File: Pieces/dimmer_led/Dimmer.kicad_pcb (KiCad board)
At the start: 2 copper layers, 67 x 56 mm, 41 parts, among them J1 Conn_01x02_Female, J2 Conn_01X03, J3 TB_1X2, J4 Conn_01x03_Female, J5 TB_1X2, J6 TB_1X2, Q1 BTA06-600C, Q2 BTA06-600C, Q3 BTA06-600C, Q5 2N7000, U1 LM78XX, U14 LM324, U3 MOC3020M, U4 MOC3020M, U5 MOC3020M, U7 PC817

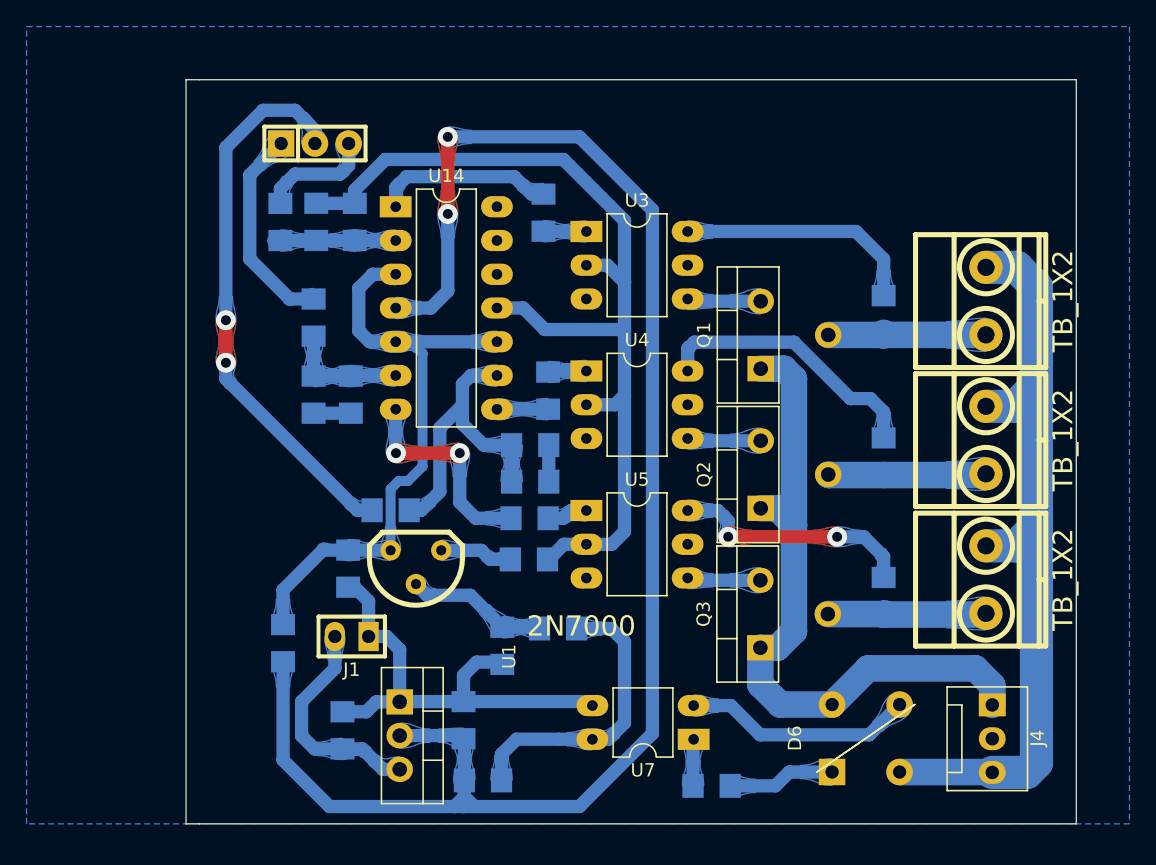
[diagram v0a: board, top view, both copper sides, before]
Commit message: dimmer actualizado
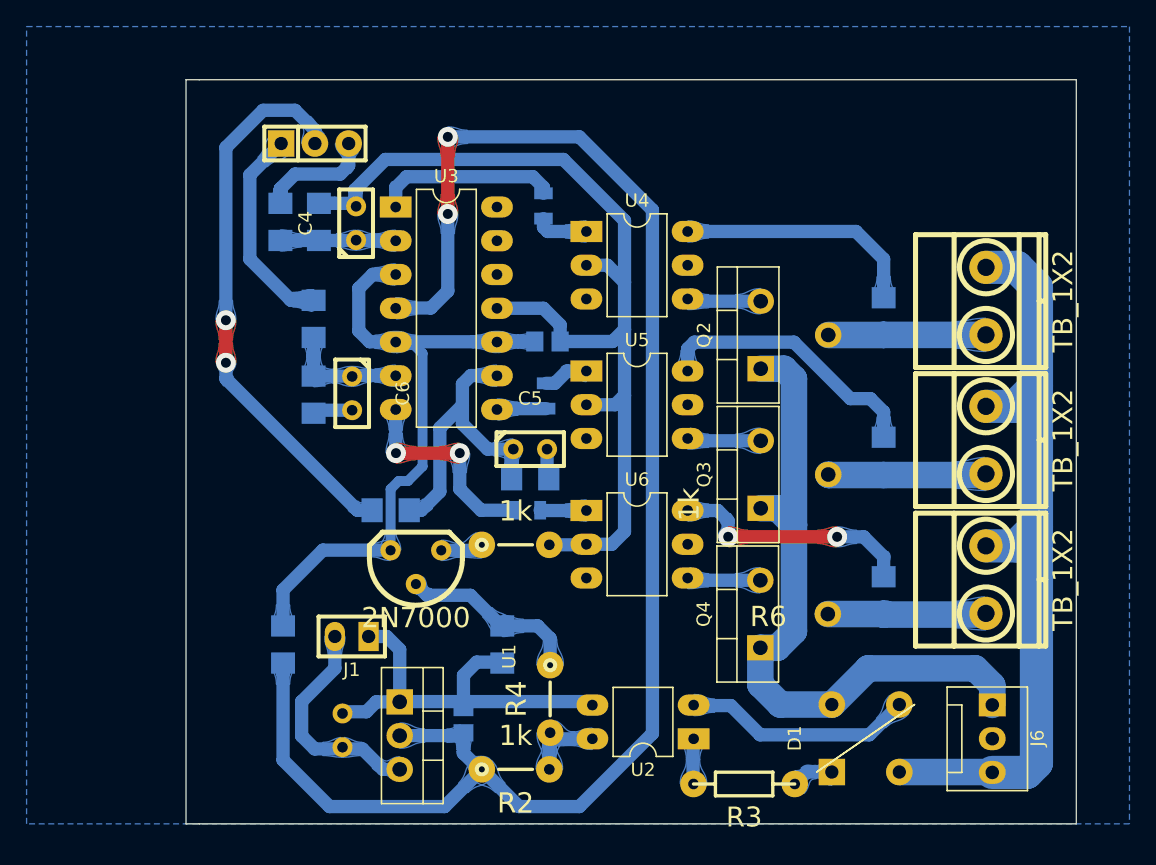
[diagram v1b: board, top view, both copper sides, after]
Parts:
- removed C20: 100nf, EESTN5:C_1206
- removed C21, C22, C23: 1uf, EESTN5:C_1206
- removed D6: D_Bridge_+A-A, EESTN5:Diode_Bridge_Round_D8.9mm
- removed Q5: 2N7000, EESTN5:to92
- removed R20, R21, R22: 220, EESTN5:R_1206
- removed R24, R25, R26: 180, EESTN5:R_1206
- removed R28: 33k, EESTN5:R_1206
- removed R29, R30, R33: 1k, EESTN5:R_1206
- removed R31, R34, R35, R38: 10k, EESTN5:R_1206
- removed R32: 100k, EESTN5:R_1206
- removed R36, R37, R46: 470k, EESTN5:R_1206
- removed U14: LM324, MacroLib:DIP-14
- removed U7: PC817, MacroLib:DIP-4
- added C3: 100nf, EESTN5:C_0805, B.Cu at (147.2, 97.7)
- added C4: 1uf, EESTN5:CAP_0.1, F.Cu at (132.8, 88.8)
- added C5: 1uf, EESTN5:CAP_0.1, F.Cu at (145.9, 105.8)
- added C6: 1uf, EESTN5:CAP_0.1, F.Cu at (132.5, 101.6)
- added D1: D_Bridge_+A-A, EESTN5:Diode_Bridge_Round_D8.9mm, F.Cu at (171.1, 127.6)
- added Q1: 2N7000, EESTN5:to92, F.Cu at (137.3, 114.0)
- added R1: 100k, EESTN5:R_1206, B.Cu at (127.3, 120.5)
- added R10: 470k, EESTN5:R_1206, B.Cu at (145.9, 108.0)
- added R11: 220, EESTN5:R_0805, B.Cu at (146.9, 87.5)
- added R12: 180, EESTN5:R_1206, B.Cu at (172.5, 95.8)
- added R13: 220, EESTN5:R_0805, B.Cu at (147.1, 101.8)
- added R14: 180, EESTN5:R_1206, B.Cu at (172.5, 106.3)
- added R15: 10k, EESTN5:R_1206, B.Cu at (129.6, 96.0)
- added R16: 220, EESTN5:R_0805, B.Cu at (145.7, 110.4)
- added R17: 180, EESTN5:R_1206, B.Cu at (172.5, 116.8)
- added R18: 470k, EESTN5:R_1206, B.Cu at (129.6, 101.7)
- added R2: 1k, EESTN5:RES0.2, F.Cu at (144.8, 129.9)
- added R3: 33k, EESTN5:RES0.3, F.Cu at (162.0, 131.0)
- added R4: 1k, EESTN5:RES0.2, F.Cu at (147.4, 124.6)
- added R5: 10k, EESTN5:R_1206, B.Cu at (143.8, 120.5)
- added R6: 1k, EESTN5:RES0.2, F.Cu at (144.8, 113.0)
- added R7: 10k, EESTN5:R_1206, B.Cu at (127.1, 88.7)
- added R8: 10k, EESTN5:R_1206, B.Cu at (135.4, 110.4)
- added R9: 470k, EESTN5:R_1206, B.Cu at (130.0, 88.7)
- added U2: PC817, MacroLib:DIP-4, F.Cu at (158.2, 127.6)
- added U3: LM324, MacroLib:DIP-14, F.Cu at (135.8, 87.6)
- C1: footprint EESTN5:C_1206 -> EESTN5:CAP_0.1
- C2: footprint EESTN5:C_1206 -> EESTN5:C_0805
- renumbered J3 to J2, J2 to J3, J5 to J4, J6 to J5, J4 to J6, Q1 to Q2, Q2 to Q3, Q3 to Q4, U3 to U4, U4 to U5, U5 to U6
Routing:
- net Net-(C5-Pad1): track 0.00 -> 24.7 mm
- net Net-(C23-Pad1): track 23.1 -> 0.00 mm
- net Net-(R29-Pad2): track 22.3 -> 0.00 mm
- net Net-(D6-Pad3): track 17.4 -> 0.00 mm
- net Net-(D1-Pad3): track 0.00 -> 17.4 mm
- net Net-(Q1-Pad2): track 0.00 -> 13.9 mm
- net Net-(Q5-Pad2): track 10.7 -> 0.00 mm
- net Net-(C6-Pad1): track 0.00 -> 9.20 mm
- net Net-(C22-Pad1): track 9.20 -> 0.00 mm
- net Net-(C21-Pad1): track 8.69 -> 0.00 mm
- net Net-(C4-Pad1): track 0.00 -> 8.68 mm
- net Net-(D6-Pad1): track 8.10 -> 0.00 mm
- net Net-(R2-Pad2): track 0.00 -> 6.30 mm
- net Net-(Q5-Pad1): track 5.48 -> 0.00 mm
- net Net-(R3-Pad2): track 0.00 -> 3.52 mm
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
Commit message: medido tds y ph
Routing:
- net GND: track 114.1 -> 114.9 mm
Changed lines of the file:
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@@
   (segment (start 133.569 125.566) (end 131.775 125.566) (width 1) (layer "B.Cu") (net 2))
   (segment (start 150.13 91.96) (end 151.71 91.96) (width 1) (layer "B.Cu") (net 2))
+  (segment (start 140.88 125.2445) (end 140.88 124.8) (width 1) (layer "B.Cu") (net 2))
   (segment (start 147.34 113) (end 150.09 113) (width 1) (layer "B.Cu") (net 2))
   (segment (start 153 101.75) (end 152.29 102.46) (width 1) (layer "B.Cu") (net 2))
+  (segment (start 150.54 125.06) (end 150.28 124.8) (width 1) (layer "B.Cu") (net 2))
   (segment (start 136.045 124.785) (end 136.08 124.82) (width 1) (layer "B.Cu") (net 2))
   (segment (start 146.9 95.2) (end 143.4 95.2) (width 1) (layer "B.Cu") (net 2))
@@
   (segment (start 150.13 112.96) (end 152.04 112.96) (width 1) (layer "B.Cu") (net 2))
   (segment (start 140.88 122.82) (end 140.88 124.8) (width 1) (layer "B.Cu") (net 2))
+  (segment (start 150.58 125.06) (end 150.54 125.06) (width 1) (layer "B.Cu") (net 2))
   (segment (start 148.1525 97.7) (end 148.1525 96.4525) (width 1) (layer "B.Cu") (net 2))
   (segment (start 153 93.25) (end 153 96.8) (width 1) (layer "B.Cu") (net 2))
